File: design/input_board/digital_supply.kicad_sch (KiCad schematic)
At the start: 16 parts, among them U3 TPS565201, U4 INA180

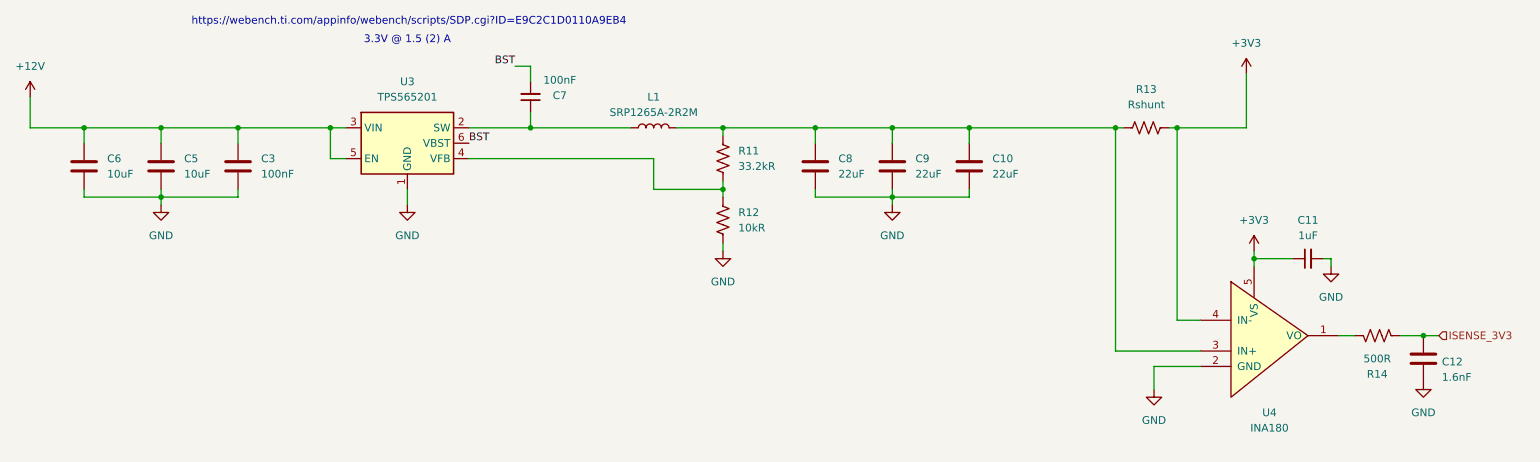
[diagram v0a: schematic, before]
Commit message: Finihs schamtic and footprints; DVDD 3.3->2V
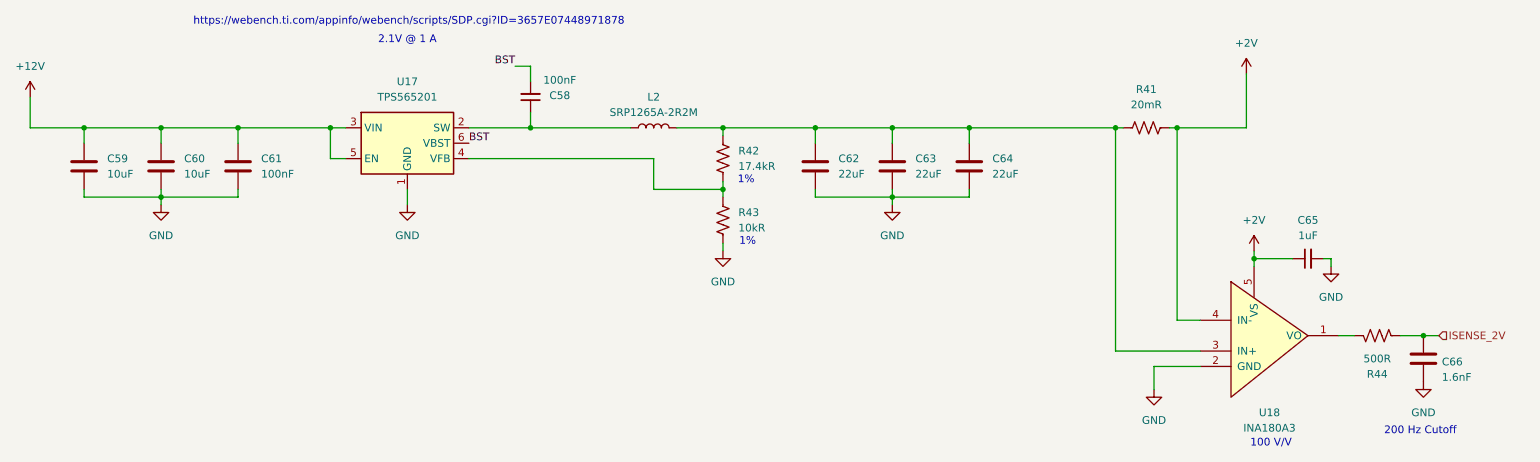
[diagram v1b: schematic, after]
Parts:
- C58: renamed from C7; footprint (none) -> Capacitor_SMD:C_0805_2012Metric_Pad1.18x1.45mm_HandSolder
- C59: renamed from C6; footprint (none) -> Capacitor_SMD:C_0805_2012Metric_Pad1.18x1.45mm_HandSolder
- C60: renamed from C5; footprint (none) -> Capacitor_SMD:C_0805_2012Metric_Pad1.18x1.45mm_HandSolder
- C61: renamed from C3; footprint (none) -> Capacitor_SMD:C_0805_2012Metric_Pad1.18x1.45mm_HandSolder
- C62: renamed from C8; footprint (none) -> Capacitor_SMD:C_0805_2012Metric_Pad1.18x1.45mm_HandSolder
- C63: renamed from C9; footprint (none) -> Capacitor_SMD:C_0805_2012Metric_Pad1.18x1.45mm_HandSolder
- C64: renamed from C10; footprint (none) -> Capacitor_SMD:C_0805_2012Metric_Pad1.18x1.45mm_HandSolder
- C65: renamed from C11; footprint (none) -> Capacitor_SMD:C_0805_2012Metric_Pad1.18x1.45mm_HandSolder
- L2: renamed from L1; footprint (none) -> input_board:IND_SRP1265A-2R2M
- R41: renamed from R13; value Rshunt -> 20mR; footprint (none) -> Resistor_SMD:R_0805_2012Metric_Pad1.20x1.40mm_HandSolder
- R42: renamed from R11; value 33.2kR -> 17.4kR; footprint (none) -> Resistor_SMD:R_0805_2012Metric_Pad1.20x1.40mm_HandSolder
- R43: renamed from R12; footprint (none) -> Resistor_SMD:R_0805_2012Metric_Pad1.20x1.40mm_HandSolder
- U18: renamed from U4; value INA180 -> INA180A3; footprint (none) -> Package_TO_SOT_SMD:SOT-23-5_HandSoldering
- renumbered C12 to C66, R14 to R44, U3 to U17
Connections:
- net +3V3 renamed +2V
- net ISENSE_3V3 renamed ISENSE_2V
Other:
- note added: "1%"
- note added: "100 V/V"
- note added: "2.1V @ 1 A"
- note added: "200 Hz Cutoff"
- note added: "https://webench.ti.com/appinfo/webench/scripts/SDP.cgi?ID=3657E07448971878"
- note removed: "3.3V @ 1.5 (2) A"
- note removed: "https://webench.ti.com/appinfo/webench/scripts/SDP.cgi?ID=E9C2C1D0110A9EB4"

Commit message: Layout v2; better
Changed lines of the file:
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@@
 	(wire
 		(pts
-			(xy 217.17 92.71) (xy 228.6 92.71)
+			(xy 217.17 92.71) (xy 254 92.71)
 		)
 		(stroke
@@
 	(wire
 		(pts
-			(xy 228.6 83.82) (xy 228.6 92.71)
+			(xy 254 83.82) (xy 254 92.71)
 		)
 		(stroke
@@
 	(symbol
 		(lib_id "input_board:+2V")
-		(at 228.6 83.82 0)
+		(at 254 83.82 0)
 		(unit 1)
 		(exclude_from_sim no)
@@
 		(fields_autoplaced yes)
 		(property "Reference" "#PWR0133"
-			(at 228.6 87.63 0)
+			(at 254 87.63 0)
 			(effects
 				(font
@@
 		)
 		(property "Value" "+2V"
-			(at 228.6 78.74 0)
+			(at 254 78.74 0)
 			(effects
 				(font
@@
 		)
 		(property "Footprint" ""
-			(at 228.6 83.82 0)
+			(at 254 83.82 0)
 			(effects
 				(font
@@
 		)
 		(property "Datasheet" ""
-			(at 228.6 83.82 0)
+			(at 254 83.82 0)
 			(effects
 				(font
@@
 		)
 		(property "Description" "Power symbol creates a global label with name \"+2V\""
-			(at 228.6 83.82 0)
-			(effects
-				(font
+			(at 254 83.82 0)
+			(effects
+				(font
